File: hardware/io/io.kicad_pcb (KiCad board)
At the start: 4 copper layers, 215 x 232 mm, 792 parts, among them J1 USB_B, J10 Conn_02x18_Odd_Even, J11 Barrel_Jack_Switch_Pin3Ring, J2 Conn_02x03_Odd_Even, J3 Conn_02x08_Odd_Even, J4 Conn_02x40_Odd_Even, J5 Conn_02x16_Odd_Even, J6 Conn_02x16_Odd_Even, J7 Conn_02x12_Odd_Even, J8 Conn_02x24_Odd_Even, Q129 IRLML6244, Q130 IRLML6402, Q131 IRLML6244, Q132 IRLML6402, Q133 IRLML6244, Q134 IRLML6402, Q135 IRLML6244, Q136 IRLML6402, Q137 IRLML6244, Q138 IRLML6402, Q139 IRLML6244, Q140 IRLML6402, Q141 IRLML6244, Q142 IRLML6402, Q143 IRLML6244, Q144 IRLML6402, Q145 IRLML6244, Q146 IRLML6402, Q147 IRLML6244, Q148 IRLML6402, Q149 IRLML6244, Q150 IRLML6402, Q151 IRLML6244, Q152 IRLML6402, Q153 IRLML6244, Q154 IRLML6402, Q155 IRLML6244, Q156 IRLML6402, Q157 IRLML6244, Q158 IRLML6402, Q159 IRLML6244, Q160 IRLML6402, Q161 IRLML6244, Q162 IRLML6402, Q163 IRLML6244, Q164 IRLML6402, Q165 IRLML6244, Q166 IRLML6402, Q167 IRLML6244, Q168 IRLML6402, Q169 IRLML6244, Q170 IRLML6402, Q171 IRLML6244, Q172 IRLML6402, Q173 IRLML6244, Q174 IRLML6402, Q175 IRLML6244, Q176 IRLML6402, Q177 IRLML6244, Q178 IRLML6402, Q179 IRLML6244, Q180 IRLML6402, Q181 IRLML6244, Q182 IRLML6402, Q183 IRLML6244, Q184 IRLML6402, Q185 IRLML6244, Q186 IRLML6402, Q187 IRLML6244, Q188 IRLML6402, Q189 IRLML6244, Q190 IRLML6402, Q191 IRLML6244, Q192 IRLML6402, Q193 IRLML6244, Q194 IRLML6402, Q195 IRLML6244, Q196 IRLML6402, Q197 IRLML6244, Q198 IRLML6402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

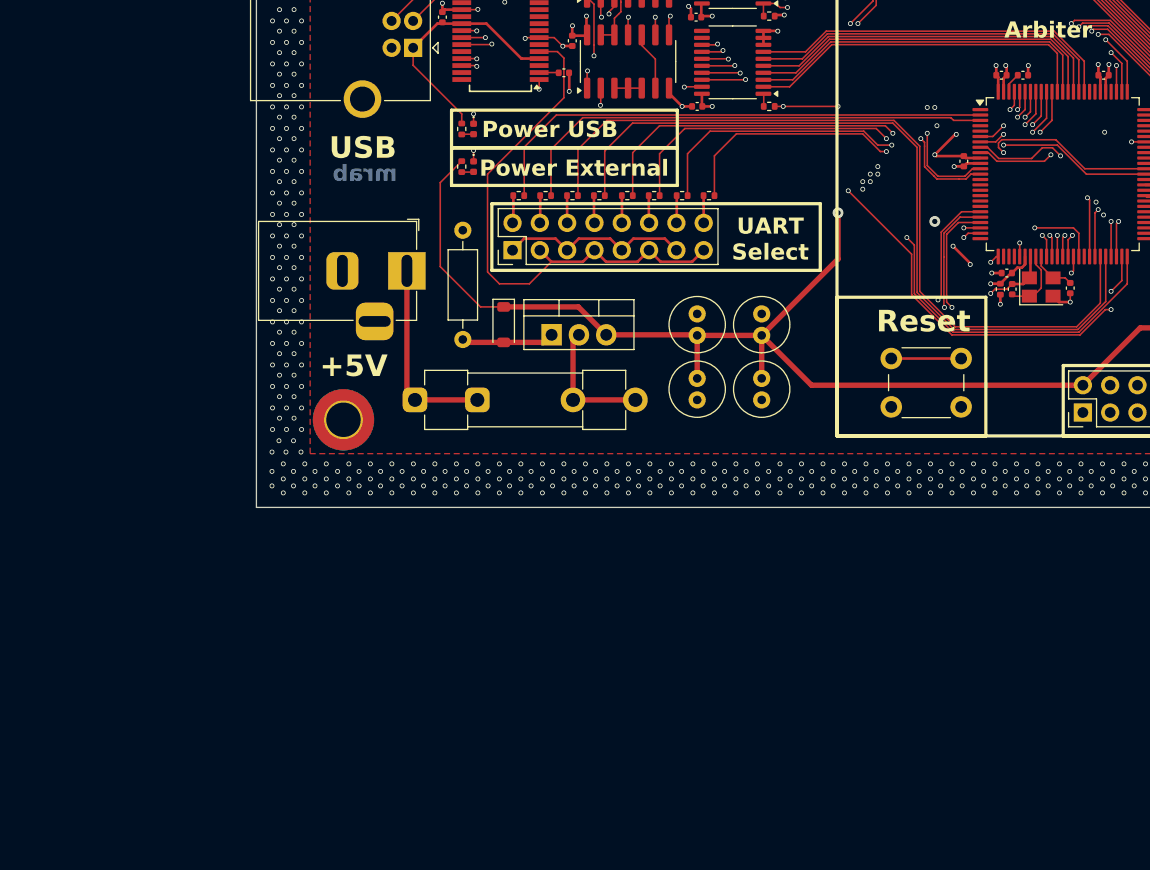
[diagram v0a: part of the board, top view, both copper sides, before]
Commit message: added Traco DCDC, not hooked up yet
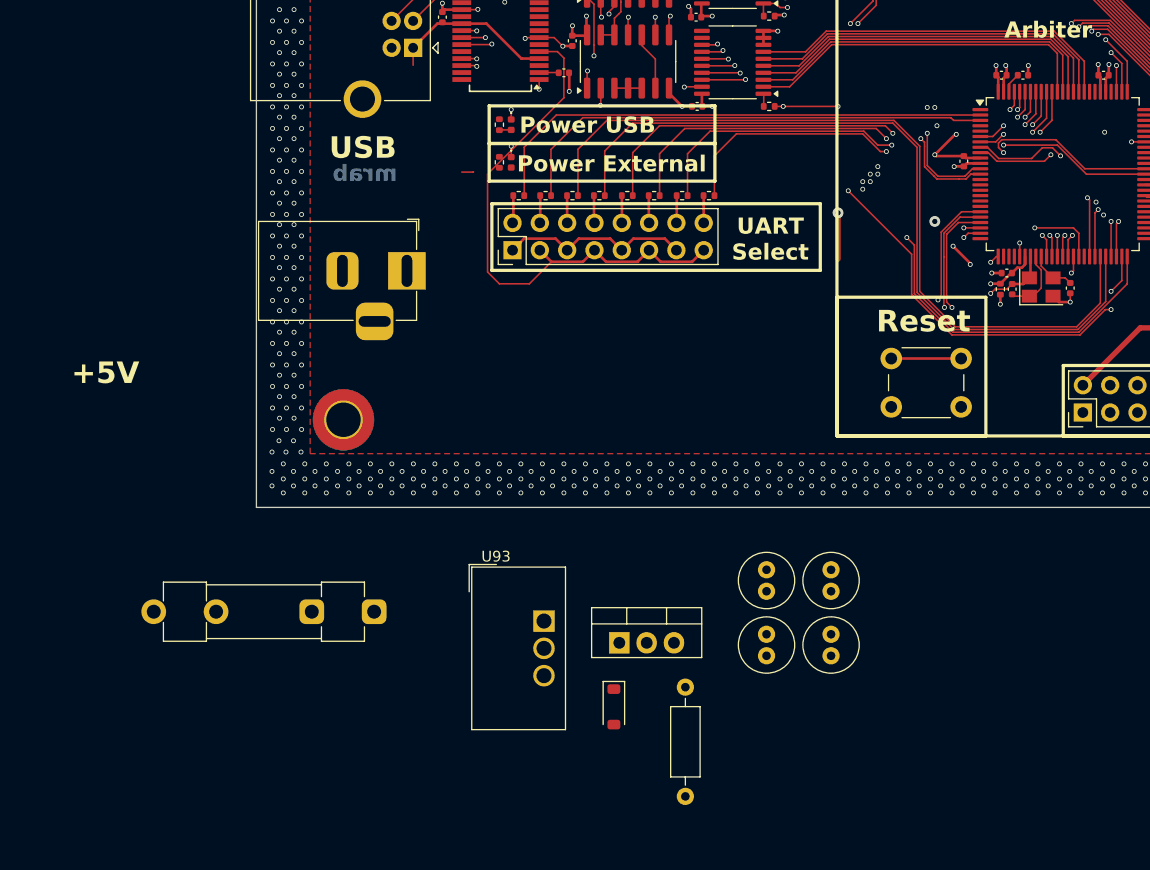
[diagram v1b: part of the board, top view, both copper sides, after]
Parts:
- added U93: TSR3-2450N, Converter_DCDC:Converter_DCDC_TRACO_TSR2-24xxN_TSR2-24xxxN_THT, F.Cu at (243.8, 500.6)
- moved R115 47.3 mm to (256.9, 516.9)
- moved D6 37.0 mm to (250.2, 508.6)
- moved Q2 29.3 mm to (250.8, 502.6)
- moved C26 24.7 mm to (270.4, 501.8)
- moved C41 24.7 mm to (270.4, 497.8)
- moved C97 24.7 mm to (264.4, 501.8)
- moved C98 24.7 mm to (264.4, 497.8)
- moved F1 20.1 mm to (227.9, 499.7), turned to 180 degrees
- moved D4 3.52 mm to (240.7, 457.9)
- moved D7 3.52 mm to (240.7, 454.4)
- moved R311 3.52 mm to (239.6, 457.9)
- moved R313 3.52 mm to (239.6, 454.4)
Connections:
- D6 pad 1: +5V -> Net-(D6-K)
- Q2 pad 3: +5V -> Net-(D6-K)
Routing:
- net +5V: track 3387.6 -> 3294.6 mm
- net Net-(F1-Pad1): track 18.1 -> 0.00 mm
- net Net-(Q2-D): track 12.1 -> 0.00 mm
- net Net-(D6-A): track 8.66 -> 0.00 mm
- net VUSB: track 43.2 -> 35.9 mm
